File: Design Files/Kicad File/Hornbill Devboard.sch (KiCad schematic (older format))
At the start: 51 parts, among them CON1 USB-MINI-B, IC1 MCP73831, M1 ESP-WROOM-32, P1 LIPO, P2 CONN_01X19, P3 CONN_01X19, Q1 IRLML5203, Q2 S8050, Q3 S8050, SW1 SW_PUSH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

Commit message: Changes done as per Issues
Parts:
- removed C4: 0.1uF, Capacitors_SMD:C_0603, symbol C
- removed R14, R15: 0E, Resistors_SMD:R_0603, symbol R
- removed U5: CP2102, EE:cp2102_xl2, symbol CP2102
- added R12, R8: 0E, Resistors_SMD:R_0603, symbol R
- added U5: CP2104, Hornbill:QFN-24-1EP_4x4mm_Pitch0.5mm, symbol CP2104-RESCUE-Hornbill_Devboard
- C3: value 0.1uF -> 10uF
- CON1: footprint EE:USB_Micro-B_SMD_NEW_1 -> Hornbill:USB_Micro-B_SMD_NEW_1
- D1: footprint EE:SOD-80_diode -> Hornbill:SOD-80_diode
- D2, D3, D4: symbol LED -> LED-RESCUE-Hornbill_Devboard
- F1: footprint Fuse_Holders_and_Fuses:Fuse_SMD1206_HandSoldering -> Capacitors_SMD:C_1206
- M1: footprint ESP32:ESP-32S -> Hornbill:ESP-32S
- P1: footprint JST:s2b-ph-kl -> Hornbill:s2b-ph-kl
- SW1, SW2: footprint SMD tactile:smd_push2 -> Hornbill:smd_push2_New
- U1: footprint walter logo:Logo_silk_OSHW_6x6mm -> Hornbill:Logo_silk_OSHW_6x6mm
- U2: footprint EE:Logo_8 -> Hornbill:Hornbill_ESP32_Dev
- U3: footprint EE:Logo_8 -> Hornbill:Logo_8
- Y1: footprint EE:SMD_RTC_Crstl -> Hornbill:SMD_RTC_Crstl
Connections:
- net +3V3: now also C3.2, U5.5 (VIO), U5.6 (VDD), U5.7 (REGIN)
- net DTR: now also U5.23 (DTR)
- net GND: now also D3.1 (K), D4.1 (K), U5.2 (GND), U5.25 (PAD)
- net IO15: now also R12.1; no longer R9.1
- net RTS: now also U5.19 (RTS)
- net RXD0: now also R8.1
- net TXD0: now also R9.1
- net VCC: now also U5.8 (VBUS); no longer C3.2
- net at R3.1: now also D3.2 (A)
- net at IC1.1 (STAT): now also D2.1 (K)
- net at R4.2: now also D2.2 (A)
- net at CON1.2 (D-): now also U5.4 (D-)
- net at CON1.3 (D+): now also U5.3 (D+)
- net at R9.2: now also U5.20 (RXD)
- net at R13.1: now also D4.2 (A)
- new net: R12.2, U5.18 (CTS)
- new net: R8.2, U5.21 (TXD)
- no-connect marks 22 -> 18
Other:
- note added: "USB to Serial Converter (CP2104)"
- note removed: "NC"
- note removed: "USB to Serial Converter (CP2102)"
- moved on the sheet: Q2, Q3, R5, R6

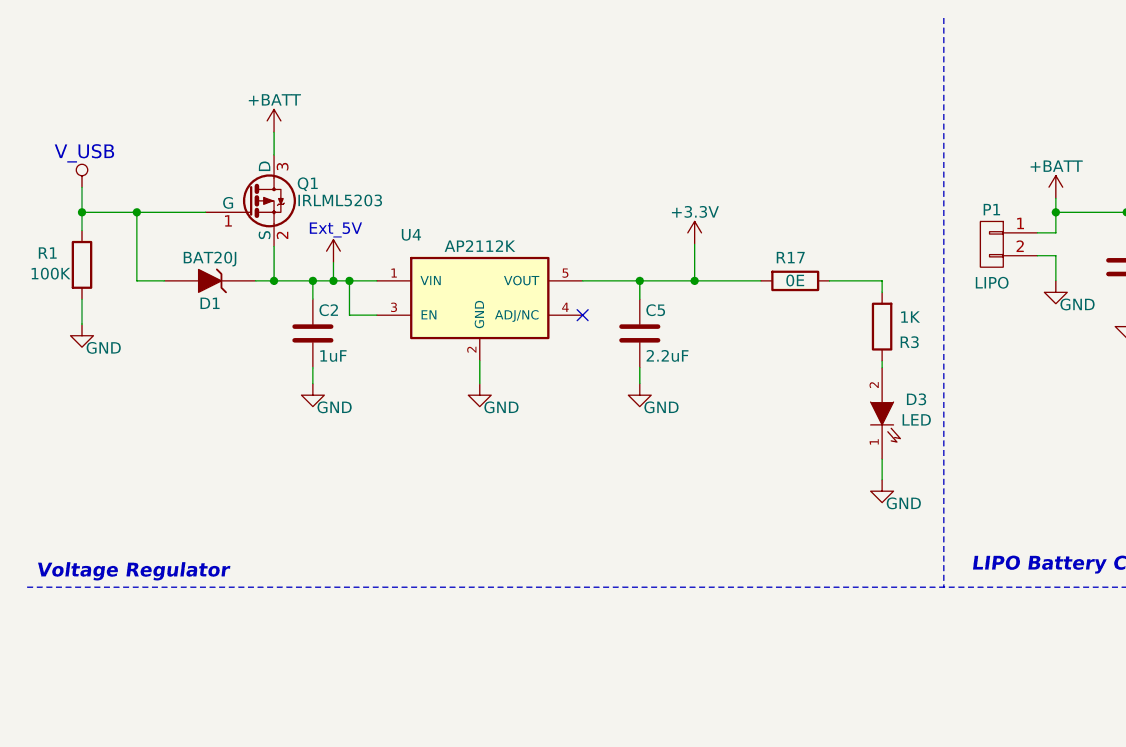
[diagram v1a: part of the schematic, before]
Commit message: Added battery monitoring Circuit
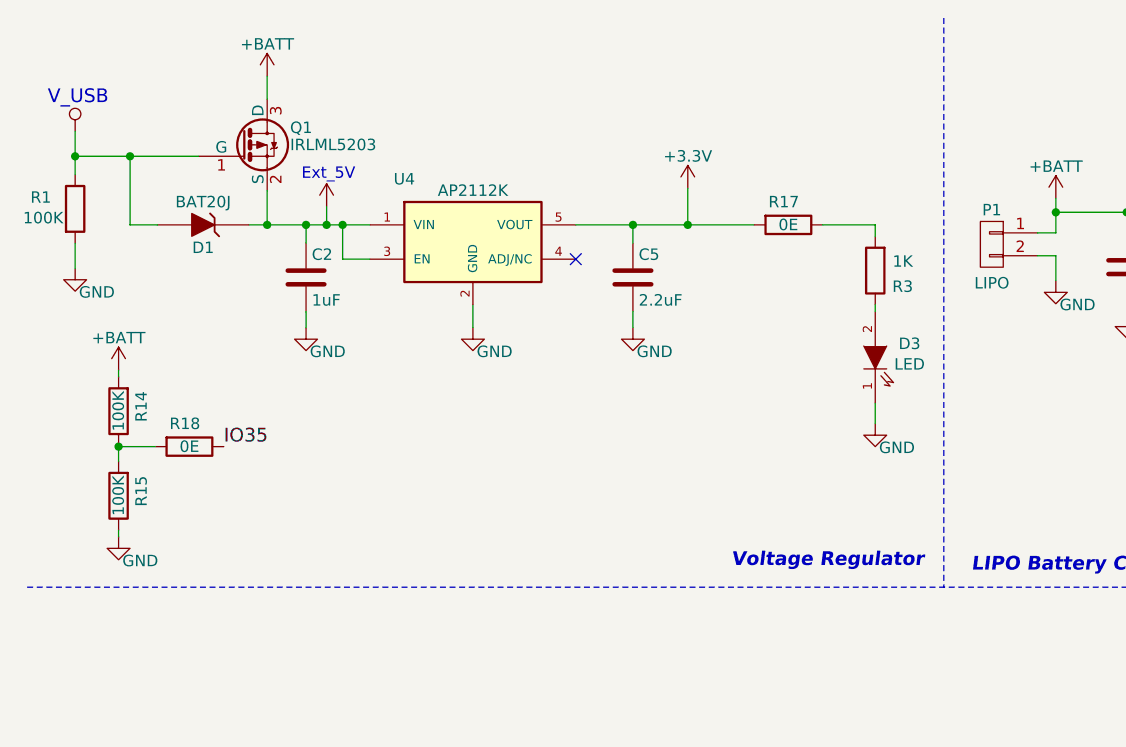
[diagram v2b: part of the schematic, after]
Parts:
- added R14, R15: 100K, Resistors_SMD:R_0603, symbol R
- added R18: 0E, Resistors_SMD:R_0603, symbol R
- P1: footprint Hornbill:s2b-ph-kl -> Hornbill:JST_SMD
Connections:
- net +BATT: now also R14.2
- net GND: now also R15.1
- net IO35: now also R18.1
- new net: R14.1, R15.2, R18.2
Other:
- moved on the sheet: C2, C5, D1, D3, Q1, R1, R17, R3, U4

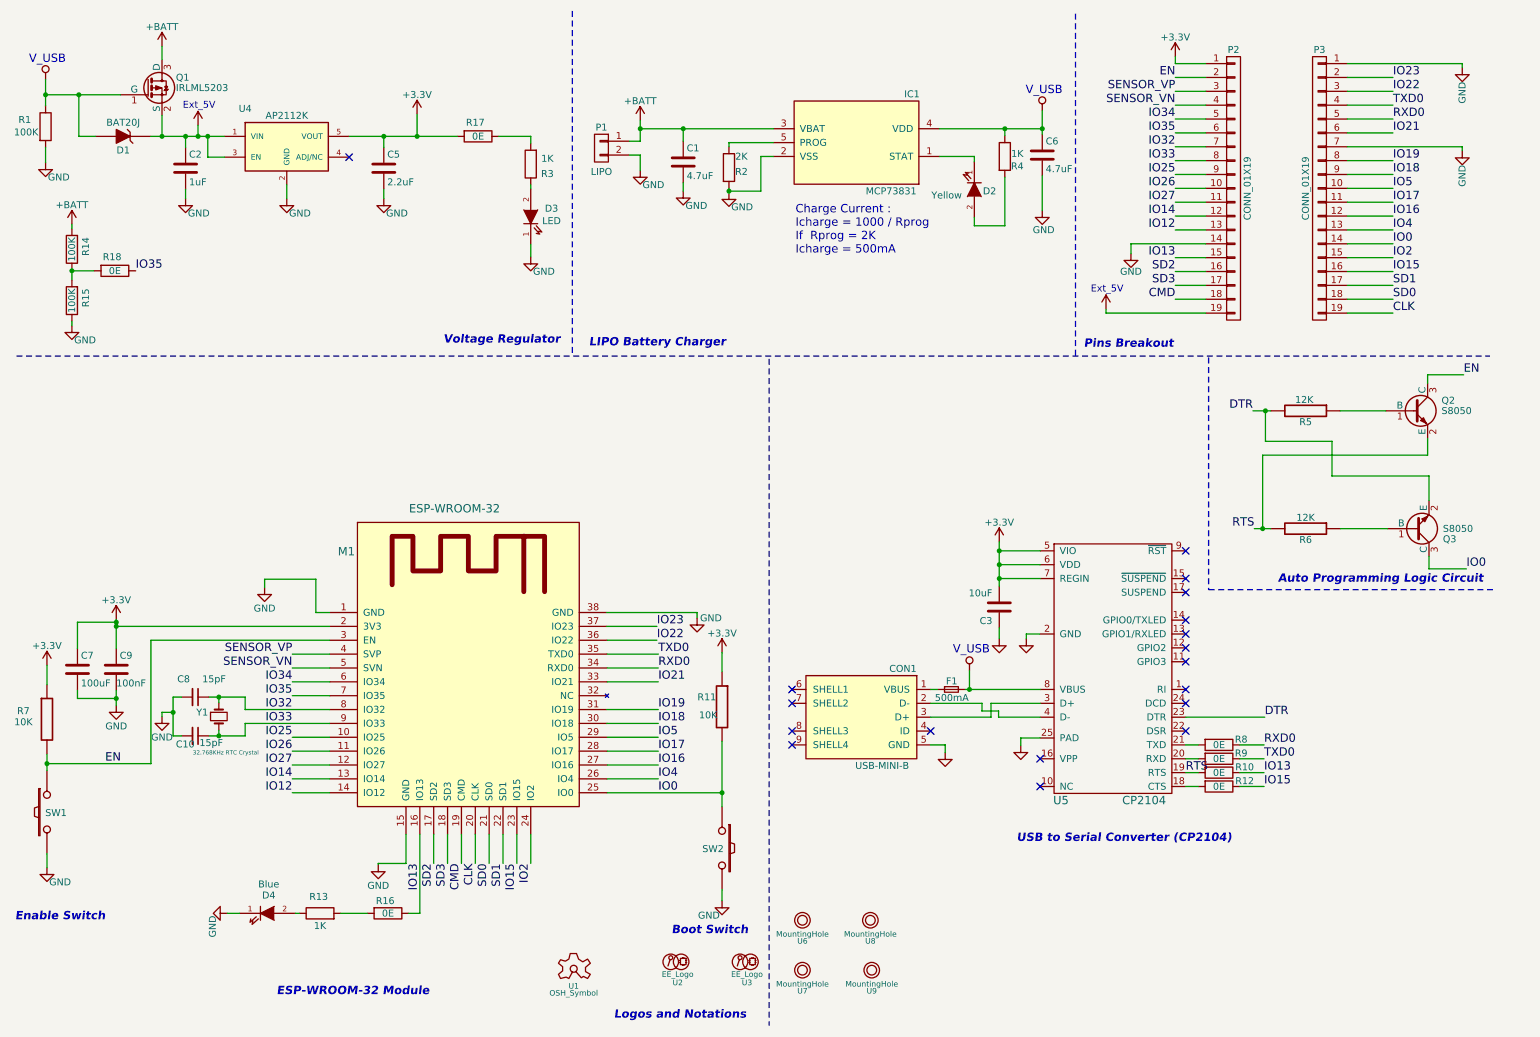
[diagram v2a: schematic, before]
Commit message: Chnged to CP2102 and LED to IO5
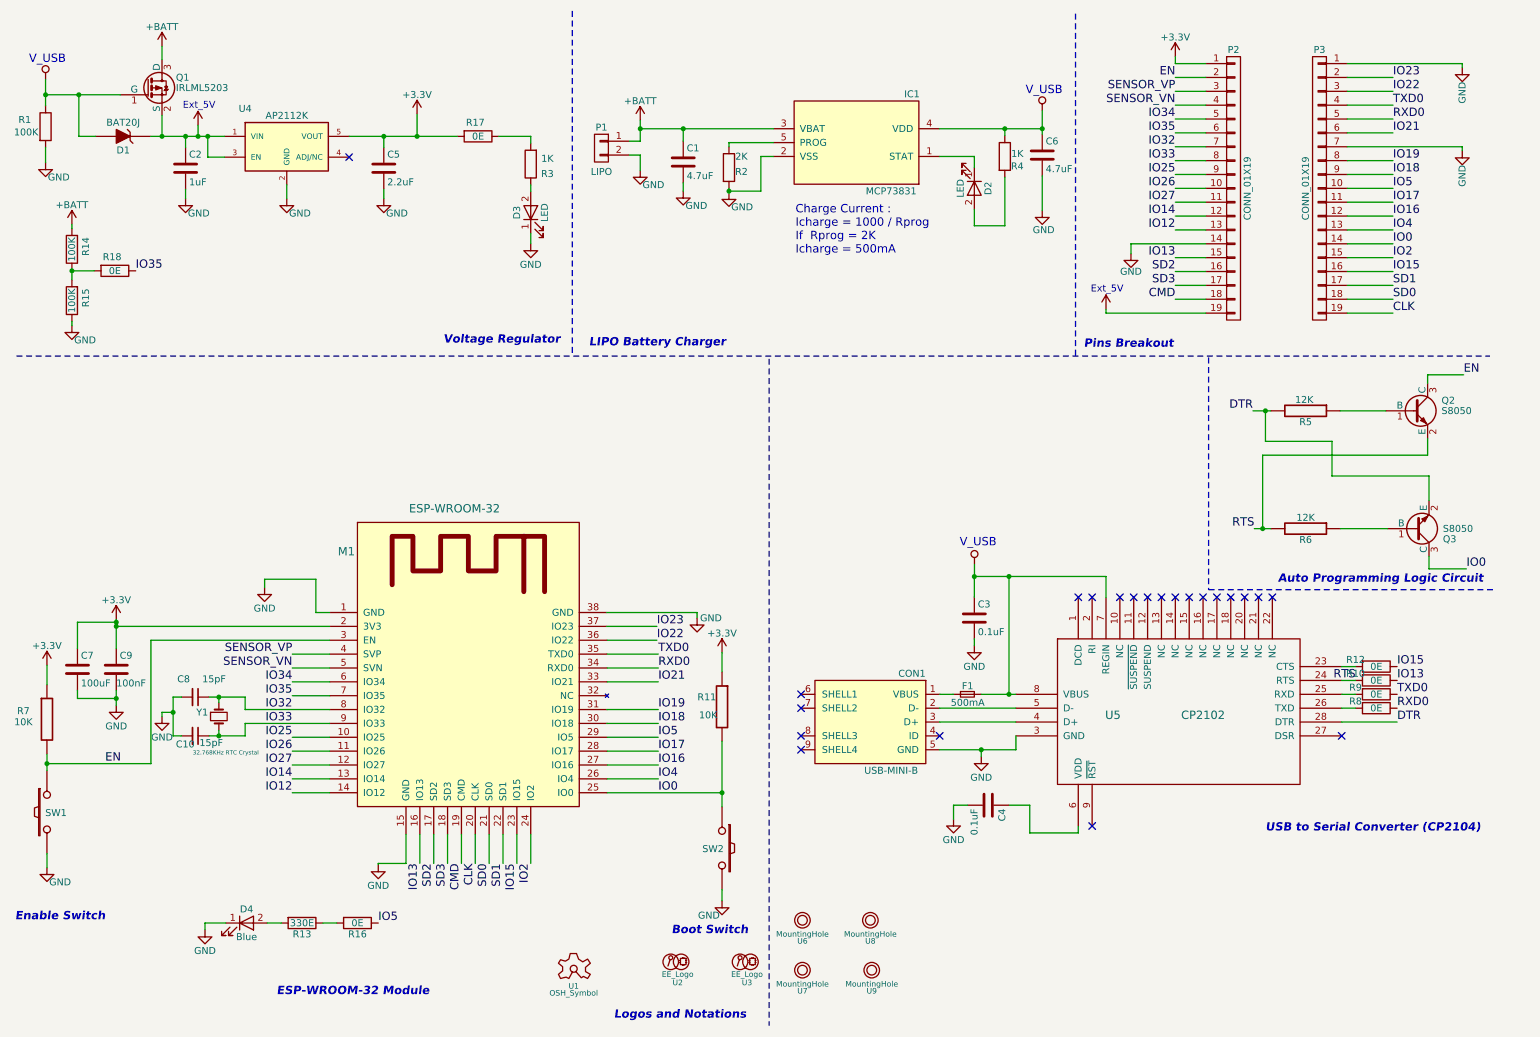
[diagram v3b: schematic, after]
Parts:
- removed D2: Yellow, LEDs:LED-0603, symbol LED-RESCUE-Hornbill_Devboard
- removed D3: LED, LEDs:LED-0603, symbol LED-RESCUE-Hornbill_Devboard
- removed D4: Blue, LEDs:LED-0603, symbol LED-RESCUE-Hornbill_Devboard
- removed U5: CP2104, Hornbill:QFN-24-1EP_4x4mm_Pitch0.5mm, symbol CP2104-RESCUE-Hornbill_Devboard
- added C4: 0.1uF, Capacitors_SMD:C_0603, symbol C
- added D2, D3: LED, Hornbill:LED-0603, symbol LED
- added D4: Blue, Hornbill:LED-0603, symbol LED
- added U5: CP2102, Hornbill:cp2102_xl2, symbol CP2102
- C3: value 10uF -> 0.1uF
- F1: footprint Capacitors_SMD:C_1206 -> Fuse_Holders_and_Fuses:Fuse_SMD1206_Wave
- R13: value 1K -> 330E
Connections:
- net +3V3: no longer C3.2
- net DTR: now also U5.28 (DTR)
- net GND: now also C3.2, C4.2, D3.1 (K), D4.1 (K), U5.3 (GND); no longer C3.1
- net IO13: no longer R16.1
- net IO5: now also R16.1
- net RTS: now also U5.24 (RTS)
- net VCC: now also C3.1, U5.7 (REGIN), U5.8 (VBUS)
- net at R3.1: now also D3.2 (A)
- net at IC1.1 (STAT): now also D2.1 (K)
- net at R4.2: now also D2.2 (A)
- net at R13.1: now also R16.2
- net at R13.2: now also D4.2 (A); no longer R16.2
- net at R12.2: now also U5.23 (CTS)
- net at R9.2: now also U5.25 (RXD)
- net at R8.2: now also U5.26 (TXD)
- net at CON1.3 (D+): now also U5.4 (D+)
- net at CON1.2 (D-): now also U5.5 (D-)
- new net: C4.1, U5.6 (VDD)
- no-connect marks 18 -> 22

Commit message: v0.3 Modified
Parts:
- removed D2, D3: LED, Hornbill:LED-0603, symbol LED
- removed D4: Blue, Hornbill:LED-0603, symbol LED
- removed F1: 500mA, Fuse_Holders_and_Fuses:Fuse_SMD1206_Wave, symbol F_Small
- added D2: Yellow, LEDs:LED-0603, symbol LED-RESCUE-Hornbill_Devboard
- added D3: LED, LEDs:LED-0603, symbol LED-RESCUE-Hornbill_Devboard
- added D4: Blue, LEDs:LED-0603, symbol LED-RESCUE-Hornbill_Devboard
- added F1: 500mA, Hornbill:Fuse_500mA, symbol Fuse
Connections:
- net GND: now also C3.1, C4.1, D3.1 (K), D4.1 (K); no longer C3.2, C4.2
- net VCC: now also C3.2, F1.1; no longer C3.1
- net at R3.1: now also D3.2 (A)
- net at IC1.1 (STAT): now also D2.1 (K)
- net at R4.2: now also D2.2 (A)
- net at U5.6 (VDD): now also C4.2; no longer C4.1
- net at CON1.1 (VBUS): now also F1.2
- net at R13.1: now also D4.2 (A); no longer R16.2
- net at R13.2: now also R16.2
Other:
- moved on the sheet: Q2, Q3, R5, R6

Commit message: v0.3 Changes1
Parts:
- removed R14, R15: 100K, Resistors_SMD:R_0603, symbol R
- removed R18: 0E, Resistors_SMD:R_0603, symbol R
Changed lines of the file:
@@
 $EndComp
-$Comp
-L R R18
-U 1 1 58941437
-P 1250 2345
-F 0 "R18" V 1150 2325 50  0000 C CNN
-F 1 "0E" V 1250 2345 50  0000 C CNN
-F 2 "Resistors_SMD:R_0603" V 1180 2345 50  0001 C CNN
-F 3 "" H 1250 2345 50  0000 C CNN
-	1    1250 2345
-	0    1    1    0
-$EndComp
-$Comp
-L R R14
-U 1 1 58941AED
-P 940 2190
-F 0 "R14" V 840 2170 50  0000 C CNN
-F 1 "100K" V 940 2190 50  0000 C CNN
-F 2 "Resistors_SMD:R_0603" V 870 2190 50  0001 C CNN
-F 3 "" H 940 2190 50  0000 C CNN
-	1    940  2190
-	-1   0    0    1
-$EndComp
-$Comp
-L R R15
-U 1 1 58942001
-P 940 2560
-F 0 "R15" V 840 2540 50  0000 C CNN
-F 1 "100K" V 940 2560 50  0000 C CNN
-F 2 "Resistors_SMD:R_0603" V 870 2560 50  0001 C CNN
-F 3 "" H 940 2560 50  0000 C CNN
-	1    940  2560
-	-1   0    0    1
-$EndComp
-$Comp
-L GND #PWR032
-U 1 1 589433F5
-P 940 2740
-F 0 "#PWR032" H 940 2490 50  0001 C CNN
-F 1 "GND" H 1035 2635 50  0000 C CNN
-F 2 "" H 940 2740 50  0000 C CNN
-F 3 "" H 940 2740 50  0000 C CNN
-	1    940  2740
-	1    0    0    -1
-$EndComp
-$Comp
-L +BATT #PWR033
-U 1 1 589452A9
-P 940 2010
-F 0 "#PWR033" H 940 1860 50  0001 C CNN
-F 1 "+BATT" H 940 2150 50  0000 C CNN
-F 2 "" H 940 2010 50  0000 C CNN
-F 3 "" H 940 2010 50  0000 C CNN
-	1    940  2010
-	1    0    0    -1
-$EndComp
-Text Label 1400 2345 0    60   ~ 0
-IO35
 $Comp
 L CP2102 U5
@@
 NoConn ~ 7100 5750
 $Comp
-L GND #PWR034
+L GND #PWR032
 U 1 1 58EC2AEE
 P 7300 6350
-F 0 "#PWR034" H 7300 6100 50  0001 C CNN
+F 0 "#PWR032" H 7300 6100 50  0001 C CNN
 F 1 "GND" H 7300 6200 50  0000 C CNN
 F 2 "" H 7300 6350 50  0000 C CNN
@@
 NoConn ~ 9500 4750
 $Comp
-L GND #PWR035
+L GND #PWR033
 U 1 1 58EC6CB9
 P 7200 5050
-F 0 "#PWR035" H 7200 4800 50  0001 C CNN
+F 0 "#PWR033" H 7200 4800 50  0001 C CNN
 F 1 "GND" H 7200 4900 50  0000 C CNN
 F 2 "" H 7200 5050 50  0000 C CNN
@@
 IO5
 $Comp
-L VCC #PWR036
+L VCC #PWR034
 U 1 1 58ECAC11
 P 7447 4477
-F 0 "#PWR036" H 7447 4327 50  0001 C CNN
+F 0 "#PWR034" H 7447 4327 50  0001 C CNN
 F 1 "VCC" H 7447 4627 50  0001 C CNN
 F 2 "" H 7447 4477 50  0000 C CNN
@@
 	9140 2970 9140 4645
 Wire Wire Line
-	1100 2345 940  2345
-Wire Wire Line
-	940  2340 940  2410
-Connection ~ 940  2345
-Wire Wire Line
-	940  2710 940  2740
-Wire Wire Line
-	940  2010 940  2040
-Wire Wire Line
 	10000 5250 10150 5250
 Wire Wire Line
@@
 	9150 4650 11200 4650
 $Comp
-L GND #PWR037
+L GND #PWR035
 U 1 1 58EB642A
 P 7400 5900
-F 0 "#PWR037" H 7400 5650 50  0001 C CNN
+F 0 "#PWR035" H 7400 5650 50  0001 C CNN
 F 1 "GND" H 7400 5750 50  0000 C CNN
 F 2 "" H 7400 5900 50  0000 C CNN

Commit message: removed short track
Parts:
- D1: footprint Hornbill:SOD-80_diode -> Hornbill:SOD-80_diode_1
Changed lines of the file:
@@
 F 0 "D1" H 1310 1475 50  0000 C CNN
 F 1 "BAT20J" H 1310 1275 50  0000 C CNN
-F 2 "Hornbill:SOD-80_diode" H 1310 1375 50  0001 C CNN
+F 2 "Hornbill:SOD-80_diode_1" H 1310 1375 50  0001 C CNN
 F 3 "" H 1310 1375 50  0000 C CNN
 	1    1310 1375
